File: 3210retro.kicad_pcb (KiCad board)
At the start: 2 copper layers, 44 x 115 mm, 24 parts, among them P109 Rumble_Pads, Q201 BC817-40, Q801 BSS138, SW701 SW_PUSH, SW702 C, SW703 1, SW704 4ghi, SW705 7pqrs, SW706 -, SW707 2abc, SW708 5jkl, SW709 8tuv, SW710 UP, SW711 3def, SW712 6mno, SW713 9wxyz, SW714 *+, SW715 DOWN, SW716 0space, SW717 #up

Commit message: aktuelle Version
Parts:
- added C201: 22p, Capacitors_SMD:C_0603, F.Cu at (225.9, 61.8)
- added C202: 22p, Capacitors_SMD:C_0603, F.Cu at (230.3, 55.9)
- added C203: 22p, Capacitors_SMD:C_0603, F.Cu at (218.9, 67.7)
- added C204: 22p, Capacitors_SMD:C_0603, F.Cu at (192.3, 95.8)
- added C205: C, Capacitors_SMD:C_0603, F.Cu at (196.7, 95.8)
- added C206: C, Capacitors_SMD:C_0603, F.Cu at (210.1, 83.0)
- added C207: 100n, Capacitors_SMD:C_0603, F.Cu at (269.6, 84.1)
- added C208: 100n, Capacitors_SMD:C_0603, F.Cu at (291.1, 67.7)
- added C209: 100n, Capacitors_SMD:C_0603, F.Cu at (274.0, 84.1)
- added C210: 100n, Capacitors_SMD:C_0603, F.Cu at (280.6, 73.6)
- added C211: 100n, Capacitors_SMD:C_0603, F.Cu at (300.3, 55.9)
- added C212: 100n, Capacitors_SMD:C_0603, F.Cu at (282.3, 67.7)
- added C213: 100n, Capacitors_SMD:C_0603, F.Cu at (295.5, 61.8)
- added C214: 100n, Capacitors_SMD:C_0603, F.Cu at (300.4, 85.4)
- added C215: 100n, Capacitors_SMD:C_0603, F.Cu at (307.0, 79.5)
- added C216: 100n, Capacitors_SMD:C_0603, F.Cu at (304.8, 85.4)
- added C217: 100n, Capacitors_SMD:C_0603, F.Cu at (287.2, 85.4)
- added C218: 100n, Capacitors_SMD:C_0603, F.Cu at (247.3, 84.0)
- added C219: 100n, Capacitors_SMD:C_0603, F.Cu at (282.3, 61.8)
- added C220: 100n, Capacitors_SMD:C_0603, F.Cu at (265.2, 80.5)
- added C221: 100n, Capacitors_SMD:C_0603, F.Cu at (256.1, 89.5)
- added C222: 100n, Capacitors_SMD:C_0603, F.Cu at (275.0, 72.3)
- added C223: 100n, Capacitors_SMD:C_0603, F.Cu at (251.7, 89.5)
- added C224: 100n, Capacitors_SMD:C_0603, F.Cu at (307.0, 73.6)
- added C225: 100n, Capacitors_SMD:C_0603, F.Cu at (287.1, 55.9)
- added C226: 10u, Capacitors_SMD:C_0603, F.Cu at (267.4, 74.6)
- added C227: 100n, Capacitors_SMD:C_0603, F.Cu at (291.5, 55.9)
- added C228: 1n, Capacitors_SMD:C_0603, F.Cu at (286.7, 61.8)
- added C229: 1u, Capacitors_SMD:C_0603, F.Cu at (271.8, 78.2)
- added C230: 1u, Capacitors_SMD:C_0603, F.Cu at (291.1, 61.8)
- added C231: 1u, Capacitors_SMD:C_0603, F.Cu at (295.9, 55.9)
- added C301: 100n, Capacitors_SMD:C_0603, F.Cu at (263.4, 126.8)
- added C302: 100n, Capacitors_SMD:C_0603, F.Cu at (258.7, 132.7)
- added C303: 100n, Capacitors_SMD:C_0603, F.Cu at (252.3, 134.9)
- added C304: 100n, Capacitors_SMD:C_0603, F.Cu at (264.4, 115.0)
- added C305: 100n, Capacitors_SMD:C_0603, F.Cu at (247.6, 138.3)
- added C306: 100n, Capacitors_SMD:C_0603, F.Cu at (243.2, 138.3)
- added C307: 100n, Capacitors_SMD:C_0603, F.Cu at (254.6, 123.1)
- added C308: 100n, Capacitors_SMD:C_0603, F.Cu at (254.6, 155.3)
- added C309: 100n, Capacitors_SMD:C_0603, F.Cu at (247.7, 168.1)
- added C310: 100n, Capacitors_SMD:C_0603, F.Cu at (259.0, 155.3)
- added C311: 100n, Capacitors_SMD:C_0603, F.Cu at (243.3, 168.1)
- added C402: 10u, Capacitors_SMD:C_0603, F.Cu at (276.2, 78.2)
- added C403: C, Capacitors_SMD:C_0603, F.Cu at (286.7, 67.7)
- added C405: 100n, Capacitors_SMD:C_0603, F.Cu at (260.8, 80.5)
- added C406: 1n, Capacitors_SMD:C_0603, F.Cu at (265.2, 86.4)
- added C408: 100n, Capacitors_SMD:C_0603, F.Cu at (293.8, 79.5)
- added C409: 100n, Capacitors_SMD:C_0603, F.Cu at (298.2, 73.6)
- added C411: C_Small, Capacitors_SMD:C_0603, F.Cu at (261.9, 74.6)
- added C412: C_Small, Capacitors_SMD:C_0603, F.Cu at (281.6, 55.9)
- added C413: 22p, Capacitors_SMD:C_0603, F.Cu at (285.0, 73.6)
- added C415: 100n, Capacitors_SMD:C_0603, F.Cu at (293.8, 73.6)
- added C701: 1p, Capacitors_SMD:C_0603, F.Cu at (182.2, 143.0)
- added C702: 2p4, Capacitors_SMD:C_0603, F.Cu at (191.6, 133.6)
- added C703: 1u, Capacitors_SMD:C_0603, F.Cu at (208.9, 115.0)
- added C704: 10u, Capacitors_SMD:C_0603, F.Cu at (213.3, 115.0)
- added C705: 100n, Capacitors_SMD:C_0603, F.Cu at (201.5, 130.2)
- added C801: 100n, Capacitors_SMD:C_0603, F.Cu at (348.1, 67.7)
- added C802: 470u, Capacitors_SMD:C_0603, F.Cu at (356.9, 55.9)
- added C803: 100n, Capacitors_SMD:C_0603, F.Cu at (352.5, 67.7)
- added C804: C, Capacitors_SMD:C_0603, F.Cu at (352.5, 61.8)
- added C805: C, Capacitors_SMD:C_0603, F.Cu at (361.3, 55.9)
- added C806: C, Capacitors_SMD:C_0603, F.Cu at (337.8, 74.6)
- added C807: C, Capacitors_SMD:C_0603, F.Cu at (348.1, 61.8)
- added C901: 10n, Capacitors_SMD:C_0603, F.Cu at (165.6, 152.3)
- added C902: 10n, Capacitors_SMD:C_0603, F.Cu at (174.2, 152.3)
- added C903: 10u, Capacitors_SMD:C_0603, F.Cu at (264.4, 120.9)
- added C904: 100n, Capacitors_SMD:C_0603, F.Cu at (268.8, 115.0)
- added D701: LED, LEDs:LED_0603, F.Cu at (313.4, 109.8)
- added D702: LED, LEDs:LED_0603, F.Cu at (317.8, 109.8)
- added D703: LED, LEDs:LED_0603, F.Cu at (322.2, 98.0)
- added D704: LED, LEDs:LED_0603, F.Cu at (322.2, 108.2)
- added D705: LED, LEDs:LED_0603, F.Cu at (322.2, 103.1)
- added D706: LED, LEDs:LED_0603, F.Cu at (310.0, 116.7)
- added L301: 100R, Resistors_SMD:R_0603, F.Cu at (259.0, 149.4)
- added L302: 100R, Resistors_SMD:R_0603, F.Cu at (254.6, 149.4)
- added L401: 4u7, Resistors_SMD:R_0603, F.Cu at (299.8, 67.7)
- added L402: 4u7, Resistors_SMD:R_0603, F.Cu at (304.2, 61.8)
- added L701: 1n3, Resistors_SMD:R_0603, F.Cu at (169.9, 152.3)
- added L702: 2n2, Resistors_SMD:R_0603, F.Cu at (177.9, 143.0)
- added L703: 0, Resistors_SMD:R_0603, F.Cu at (161.3, 152.3)
- added L704: 1n8, Resistors_SMD:R_0603, F.Cu at (208.8, 120.9)
- added P102: BAT, Pin_Headers:Pin_Header_Straight_2x01, F.Cu at (153.0, 165.7)
- added P103: DC, Pin_Headers:Pin_Header_Straight_2x01, F.Cu at (153.0, 173.9)
- added P105: EAR, Pin_Headers:Pin_Header_Straight_2x01, F.Cu at (159.7, 165.7)
- added P106: MIC, Pin_Headers:Pin_Header_Straight_2x01, F.Cu at (159.7, 173.9)
- added P107: HEADPHONE, Pin_Headers:Pin_Header_Straight_1x04, F.Cu at (141.7, 165.7)
- added P108: LSPK, Pin_Headers:Pin_Header_Straight_1x02, F.Cu at (148.6, 165.7)
- added P701: WL_DBG, Pin_Headers:Pin_Header_Straight_1x02, F.Cu at (148.2, 118.2)
- added P702: WL_RS232, Pin_Headers:Pin_Header_Straight_1x03, F.Cu at (141.0, 118.2)
- added P703: BT_DBG, Pin_Headers:Pin_Header_Straight_1x02, F.Cu at (140.0, 131.5)
- added P801: JTAG, Pin_Headers:Pin_Header_Straight_2x05_Pitch1.27mm, F.Cu at (139.0, 55.7)
- added Q301: BC849, TO_SOT_Packages_SMD:SOT-23, F.Cu at (238.4, 168.4)
- added R201: 10, Resistors_SMD:R_0603, F.Cu at (187.9, 93.3)
- added R202: 10, Resistors_SMD:R_0603, F.Cu at (183.5, 99.2)
- added R203: 10, Resistors_SMD:R_0603, F.Cu at (225.9, 55.9)
- added R204: 10, Resistors_SMD:R_0603, F.Cu at (214.5, 65.3)
- added R205: 10, Resistors_SMD:R_0603, F.Cu at (194.6, 89.9)
- added R206: 10, Resistors_SMD:R_0603, F.Cu at (199.0, 89.9)
- added R207: 100, Resistors_SMD:R_0603, F.Cu at (214.5, 71.2)
- added R208: 100, Resistors_SMD:R_0603, F.Cu at (187.9, 99.2)
- added R209: 10k, Resistors_SMD:R_0603, F.Cu at (152.1, 102.6)
- added R210: 10k, Resistors_SMD:R_0603, F.Cu at (210.1, 65.3)
- added R211: 100, Resistors_SMD:R_0603, F.Cu at (194.6, 84.0)
- added R212: 100, Resistors_SMD:R_0603, F.Cu at (205.7, 71.2)
- added R213: 100, Resistors_SMD:R_0603, F.Cu at (221.5, 55.9)
- added R214: 100, Resistors_SMD:R_0603, F.Cu at (199.0, 84.0)
- added R215: 100, Resistors_SMD:R_0603, F.Cu at (156.5, 102.6)
- added R216: 100, Resistors_SMD:R_0603, F.Cu at (160.9, 102.6)
- added R217: 100, Resistors_SMD:R_0603, F.Cu at (212.2, 88.9)
- added R218: 100, Resistors_SMD:R_0603, F.Cu at (169.7, 102.6)
- added R219: 100, Resistors_SMD:R_0603, F.Cu at (205.7, 65.3)
- added R220: 100, Resistors_SMD:R_0603, F.Cu at (183.5, 93.3)
- added R221: 100, Resistors_SMD:R_0603, F.Cu at (147.7, 102.6)
- added R222: 100, Resistors_SMD:R_0603, F.Cu at (214.5, 83.0)
- added R223: R, Resistors_SMD:R_0603, F.Cu at (221.0, 85.4)
- added R224: R, Resistors_SMD:R_0603, F.Cu at (216.6, 88.9)
- added R225: 100, Resistors_SMD:R_0603, F.Cu at (232.1, 73.6)
- added R226: 100, Resistors_SMD:R_0603, F.Cu at (165.3, 102.6)
- added R227: 10k, Resistors_SMD:R_0603, F.Cu at (174.1, 102.6)
- added R228: 100, Resistors_SMD:R_0603, F.Cu at (203.4, 94.8)
- added R229: 100, Resistors_SMD:R_0603, F.Cu at (210.1, 77.1)
- added R230: 100, Resistors_SMD:R_0603, F.Cu at (178.5, 102.6)
- added R231: 100, Resistors_SMD:R_0603, F.Cu at (232.1, 67.7)
- added R232: 100, Resistors_SMD:R_0603, F.Cu at (223.3, 73.6)
- added R233: 100, Resistors_SMD:R_0603, F.Cu at (227.7, 67.7)
- added R234: 100, Resistors_SMD:R_0603, F.Cu at (214.5, 77.1)
- added R235: 100, Resistors_SMD:R_0603, F.Cu at (223.3, 79.5)
- added R236: 100, Resistors_SMD:R_0603, F.Cu at (203.4, 88.9)
- added R237: 100, Resistors_SMD:R_0603, F.Cu at (187.3, 105.1)
- added R238: 100, Resistors_SMD:R_0603, F.Cu at (196.7, 101.7)
- added R239: 100, Resistors_SMD:R_0603, F.Cu at (205.7, 83.0)
- added R240: 100, Resistors_SMD:R_0603, F.Cu at (207.8, 88.9)
- added R241: 100, Resistors_SMD:R_0603, F.Cu at (218.9, 79.5)
- added R242: 100, Resistors_SMD:R_0603, F.Cu at (182.9, 105.1)
- added R243: 100, Resistors_SMD:R_0603, F.Cu at (227.7, 73.6)
- added R244: 100, Resistors_SMD:R_0603, F.Cu at (207.8, 94.8)
- added R245: 100, Resistors_SMD:R_0603, F.Cu at (201.1, 100.7)
- added R246: 100, Resistors_SMD:R_0603, F.Cu at (221.5, 61.8)
- added R247: 100, Resistors_SMD:R_0603, F.Cu at (210.1, 71.2)
- added R248: 100, Resistors_SMD:R_0603, F.Cu at (205.7, 77.1)
- added R249: 0, Resistors_SMD:R_0603, F.Cu at (282.8, 85.4)
- added R301: 4k7, Resistors_SMD:R_0603, F.Cu at (259.0, 167.1)
- added R302: 0, Resistors_SMD:R_0603, F.Cu at (263.4, 161.2)
- added R303: 0, Resistors_SMD:R_0603, F.Cu at (267.8, 155.3)
- added R304: 22, Resistors_SMD:R_0603, F.Cu at (254.6, 167.1)
- added R305: 100, Resistors_SMD:R_0603, F.Cu at (259.0, 161.2)
- added R306: 100, Resistors_SMD:R_0603, F.Cu at (263.4, 155.3)
- added R307: 100, Resistors_SMD:R_0603, F.Cu at (267.8, 149.4)
- added R308: 100, Resistors_SMD:R_0603, F.Cu at (263.4, 149.4)
- added R309: 100, Resistors_SMD:R_0603, F.Cu at (254.6, 161.2)
- added R401: R, Resistors_SMD:R_0603, F.Cu at (289.4, 79.5)
- added R402: R, Resistors_SMD:R_0603, F.Cu at (278.4, 85.4)
- added R403: R, Resistors_SMD:R_0603, F.Cu at (304.7, 55.9)
- added R404: R, Resistors_SMD:R_0603, F.Cu at (295.5, 67.7)
- added R405: R, Resistors_SMD:R_0603, F.Cu at (299.9, 61.8)
- added R406: R, Resistors_SMD:R_0603, F.Cu at (285.0, 79.5)
- added R407: R, Resistors_SMD:R_0603, F.Cu at (289.4, 73.6)
- added R408: R, Resistors_SMD:R_0603, F.Cu at (302.6, 73.6)
- added R409: R, Resistors_SMD:R_0603, F.Cu at (280.6, 79.5)
- added R410: R, Resistors_SMD:R_0603, F.Cu at (296.0, 85.4)
- added R412: R, Resistors_SMD:R_0603, F.Cu at (302.6, 79.5)
- added R413: R, Resistors_SMD:R_0603, F.Cu at (291.6, 85.4)
- added R414: R, Resistors_SMD:R_0603, F.Cu at (298.2, 79.5)
- added R415: R, Resistors_SMD:R_0603, F.Cu at (260.8, 86.4)
- added R416: 0, Resistors_SMD:R_0603, F.Cu at (304.1, 67.7)
- added R601: 100, Resistors_SMD:R_0603, F.Cu at (197.1, 124.3)
- added R602: 100, Resistors_SMD:R_0603, F.Cu at (201.5, 124.3)
- added R701: 10k, Resistors_SMD:R_0603, F.Cu at (301.2, 117.1)
- added R702: 280, Resistors_SMD:R_0603, F.Cu at (313.4, 104.3)
- added R703: 0, Resistors_SMD:R_0603, F.Cu at (197.1, 130.2)
- added R704: 280, Resistors_SMD:R_0603, F.Cu at (305.6, 117.1)
- added R705: 0, Resistors_SMD:R_0603, F.Cu at (200.4, 142.0)
- added R706: 280, Resistors_SMD:R_0603, F.Cu at (313.4, 98.4)
- added R707: 0, Resistors_SMD:R_0603, F.Cu at (191.6, 139.5)
- added R708: 280, Resistors_SMD:R_0603, F.Cu at (296.8, 117.1)
- added R709: 0, Resistors_SMD:R_0603, F.Cu at (205.9, 132.7)
- added R710: 280, Resistors_SMD:R_0603, F.Cu at (317.8, 98.4)
- added R711: 100k, Resistors_SMD:R_0603, F.Cu at (210.3, 126.8)
- added R712: 280, Resistors_SMD:R_0603, F.Cu at (317.8, 104.3)
- added R801: 22, Resistors_SMD:R_0603, F.Cu at (352.5, 73.6)
- added R802: 100, Resistors_SMD:R_0603, F.Cu at (361.3, 73.6)
- added R803: 100, Resistors_SMD:R_0603, F.Cu at (356.9, 73.6)
- added R804: 100, Resistors_SMD:R_0603, F.Cu at (351.0, 79.5)
- added R805: 100, Resistors_SMD:R_0603, F.Cu at (361.3, 67.7)
- added R806: 100, Resistors_SMD:R_0603, F.Cu at (346.6, 79.5)
- added R807: 100, Resistors_SMD:R_0603, F.Cu at (356.9, 67.7)
- added R808: 100, Resistors_SMD:R_0603, F.Cu at (361.3, 61.8)
- added R809: 100, Resistors_SMD:R_0603, F.Cu at (348.1, 73.6)
- added R810: 100, Resistors_SMD:R_0603, F.Cu at (355.4, 79.5)
- added R811: 1M, Resistors_SMD:R_0603, F.Cu at (356.9, 61.8)
- added R812: 0, Resistors_SMD:R_0603, F.Cu at (348.1, 55.9)
- added R813: 100, Resistors_SMD:R_0603, F.Cu at (342.2, 74.6)
- added R814: 0, Resistors_SMD:R_0603, F.Cu at (352.5, 55.9)
- added R815: 0, Resistors_SMD:R_0603, F.Cu at (230.3, 61.8)
- added R816: 100, Resistors_SMD:R_0603, F.Cu at (218.9, 73.6)
- added R817: 100, Resistors_SMD:R_0603, F.Cu at (223.3, 67.7)
- added R818: 100, Resistors_SMD:R_0603, F.Cu at (192.3, 101.7)
- added R901: 100, Resistors_SMD:R_0603, F.Cu at (196.0, 142.0)
- added R902: 100, Resistors_SMD:R_0603, F.Cu at (205.9, 126.8)
- added R903: 100, Resistors_SMD:R_0603, F.Cu at (187.4, 148.9)
- added R904: R, Resistors_SMD:R_0603, F.Cu at (200.4, 136.1)
- added R905: 100, Resistors_SMD:R_0603, F.Cu at (213.1, 120.9)
- added R906: 100, Resistors_SMD:R_0603, F.Cu at (183.0, 148.9)
- added R907: 100, Resistors_SMD:R_0603, F.Cu at (196.0, 136.1)
- added R908: 100, Resistors_SMD:R_0603, F.Cu at (178.6, 148.9)
- added R909: 100, Resistors_SMD:R_0603, F.Cu at (186.6, 143.0)
- added R910: 10k, Resistors_SMD:R_0603, F.Cu at (254.3, 129.0)
- added R911: 10, Resistors_SMD:R_0603, F.Cu at (259.0, 126.8)
- added R912: 10, Resistors_SMD:R_0603, F.Cu at (268.8, 120.9)
- added R913: 10, Resistors_SMD:R_0603, F.Cu at (260.0, 120.9)
- added R914: 22, Resistors_SMD:R_0603, F.Cu at (243.5, 132.4)
- added R915: 10, Resistors_SMD:R_0603, F.Cu at (260.0, 115.0)
- added R916: 10, Resistors_SMD:R_0603, F.Cu at (247.9, 132.4)
- added RP901: 100, Resistors_SMD:R_Array_Convex_8x0602, F.Cu at (255.1, 116.1)
- added RP902: 100, Resistors_SMD:R_Array_Convex_8x0602, F.Cu at (232.9, 134.7)
- added RP903: 100, Resistors_SMD:R_Array_Convex_8x0602, F.Cu at (244.0, 125.4)
- added RP904: 100, Resistors_SMD:R_Array_Convex_8x0602, F.Cu at (249.4, 125.4)
- added RP905: 100, Resistors_SMD:R_Array_Convex_8x0602, F.Cu at (238.3, 134.7)
- added TP201: TP, buttons:TP, F.Cu at (270.0, 66.9)
- added TP202: TP, buttons:TP, F.Cu at (247.9, 57.5)
- added TP203: TP, buttons:TP, F.Cu at (242.3, 76.2)
- added TP204: TP, buttons:TP, F.Cu at (247.9, 76.2)
- added TP205: TP, buttons:TP, F.Cu at (242.3, 57.5)
- added TP206: TP, buttons:TP, F.Cu at (258.9, 57.5)
- added TP207: TP, buttons:TP, F.Cu at (264.5, 57.5)
- added TP208: TP, buttons:TP, F.Cu at (270.0, 57.5)
- added TP209: TP, buttons:TP, F.Cu at (275.6, 57.5)
- added TP210: TP, buttons:TP, F.Cu at (258.9, 66.9)
- added TP211: TP, buttons:TP, F.Cu at (264.5, 66.9)
- added TP212: TP, buttons:TP, F.Cu at (253.4, 66.9)
- added TP213: TP, buttons:TP, F.Cu at (242.3, 85.6)
- added TP214: TP, buttons:TP, F.Cu at (242.3, 66.9)
- added TP215: TP, buttons:TP, F.Cu at (253.4, 57.5)
- added TP216: TP, buttons:TP, F.Cu at (247.9, 66.9)
- added TP301: TP, buttons:TP, F.Cu at (233.0, 151.0)
- added TP302: TP, buttons:TP, F.Cu at (227.4, 160.4)
- added TP303: TP, buttons:TP, F.Cu at (233.0, 160.4)
- added TP304: TP, buttons:TP, F.Cu at (238.5, 151.0)
- added TP305: TP, buttons:TP, F.Cu at (221.9, 169.7)
- added TP306: TP, buttons:TP, F.Cu at (249.6, 160.4)
- added TP307: TP, buttons:TP, F.Cu at (221.9, 151.0)
- added TP308: TP, buttons:TP, F.Cu at (244.1, 160.4)
- added TP309: TP, buttons:TP, F.Cu at (233.0, 169.7)
- added TP310: TP, buttons:TP, F.Cu at (227.4, 169.7)
- added TP311: TP, buttons:TP, F.Cu at (238.5, 160.4)
- added TP312: TP, buttons:TP, F.Cu at (249.6, 151.0)
- added TP313: TP, buttons:TP, F.Cu at (227.4, 151.0)
- added TP314: TP, buttons:TP, F.Cu at (244.1, 151.0)
- added TP315: TP, buttons:TP, F.Cu at (221.9, 160.4)
- added TP501: TP, buttons:TP, F.Cu at (315.4, 57.5)
- added TP502: TP, buttons:TP, F.Cu at (337.6, 66.9)
- added TP503: TP, buttons:TP, F.Cu at (326.5, 76.2)
- added TP504: TP, buttons:TP, F.Cu at (321.0, 76.2)
- added TP505: TP, buttons:TP, F.Cu at (332.1, 66.9)
- added TP506: TP, buttons:TP, F.Cu at (343.1, 57.5)
- added TP507: TP, buttons:TP, F.Cu at (337.6, 57.5)
- added TP508: TP, buttons:TP, F.Cu at (343.1, 66.9)
- added TP509: TP, buttons:TP, F.Cu at (332.1, 57.5)
- added TP510: TP, buttons:TP, F.Cu at (326.5, 66.9)
- added TP511: TP, buttons:TP, F.Cu at (321.0, 66.9)
- added TP512: TP, buttons:TP, F.Cu at (326.5, 57.5)
- added TP513: TP, buttons:TP, F.Cu at (315.4, 76.2)
- added TP514: TP, buttons:TP, F.Cu at (321.0, 57.5)
- added TP515: TP, buttons:TP, F.Cu at (315.4, 66.9)
- added TP601: TP, buttons:TP, F.Cu at (167.5, 144.6)
- added TP602: TP, buttons:TP, F.Cu at (186.6, 125.9)
- added TP701: TP, buttons:TP, F.Cu at (186.6, 135.2)
- added TP702: TP, buttons:TP, F.Cu at (173.0, 144.6)
- added TP703: TP, buttons:TP, F.Cu at (192.2, 125.9)
- added TP704: TP, buttons:TP, F.Cu at (204.0, 116.6)
- added TP705: TP, buttons:TP, F.Cu at (198.4, 116.6)
- added TP706: TP, buttons:TP, F.Cu at (181.1, 135.2)
- added TP707: TP, buttons:TP, F.Cu at (192.9, 116.6)
- added TP708: TP, buttons:TP, F.Cu at (175.5, 135.2)
- added TP709: TP, buttons:TP, F.Cu at (151.4, 136.7)
- added TP710: TP, buttons:TP, F.Cu at (147.8, 127.3)
- added TP711: TP, buttons:TP, F.Cu at (145.3, 146.0)
- added TP712: TP, buttons:TP, F.Cu at (150.8, 146.0)
- added TP713: TP, buttons:TP, F.Cu at (164.5, 135.2)
- added TP714: TP, buttons:TP, F.Cu at (170.0, 135.2)
- added TP715: TP, buttons:TP, F.Cu at (156.4, 146.0)
- added TP716: TP, buttons:TP, F.Cu at (187.3, 116.6)
- added TP717: TP, buttons:TP, F.Cu at (181.1, 125.9)
- added TP718: TP, buttons:TP, F.Cu at (161.9, 144.6)
- added TP719: TP, buttons:TP, F.Cu at (181.8, 116.6)
- added TP720: TP, buttons:TP, F.Cu at (175.5, 125.9)
- added TP721: TP, buttons:TP, F.Cu at (176.3, 116.6)
- added TP722: TP, buttons:TP, F.Cu at (170.7, 116.6)
- added TP723: TP, buttons:TP, F.Cu at (139.8, 140.6)
- added TP724: TP, buttons:TP, F.Cu at (170.0, 125.9)
- added TP725: TP, buttons:TP, F.Cu at (164.5, 125.9)
- added TP726: TP, buttons:TP, F.Cu at (158.9, 125.9)
- added TP727: TP, buttons:TP, F.Cu at (165.2, 116.6)
- added TP728: TP, buttons:TP, F.Cu at (159.6, 116.6)
- added TP729: TP, buttons:TP, F.Cu at (145.8, 136.7)
- added TP730: TP, buttons:TP, F.Cu at (153.4, 127.3)
- added TP731: TP, buttons:TP, F.Cu at (158.9, 135.2)
- added TP732: TP, buttons:TP, F.Cu at (154.1, 116.6)
- added TP733: TP, buttons:TP, F.Cu at (139.8, 150.0)
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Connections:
- net /Buttons and LEDs/COL_1 renamed /Buttons and LEDs/KEY0
- net /Buttons and LEDs/COL_2 renamed /Buttons and LEDs/KEY1
- net /Buttons and LEDs/COL_3 renamed /Buttons and LEDs/KEY2
- net /Buttons and LEDs/COL_4 renamed /Buttons and LEDs/KEY3
- net /Buttons and LEDs/ROW_1 renamed /Buttons and LEDs/KEY4
- net /Buttons and LEDs/ROW_2 renamed /Buttons and LEDs/KEY5
- net /Buttons and LEDs/ROW_3 renamed /Buttons and LEDs/KEY6
- net /Buttons and LEDs/ROW_4 renamed /Buttons and LEDs/KEY7
- P109 pad 1: (no net) -> /Audio Amplifier/RMBL+
- P109 pad 2: (no net) -> +3V3

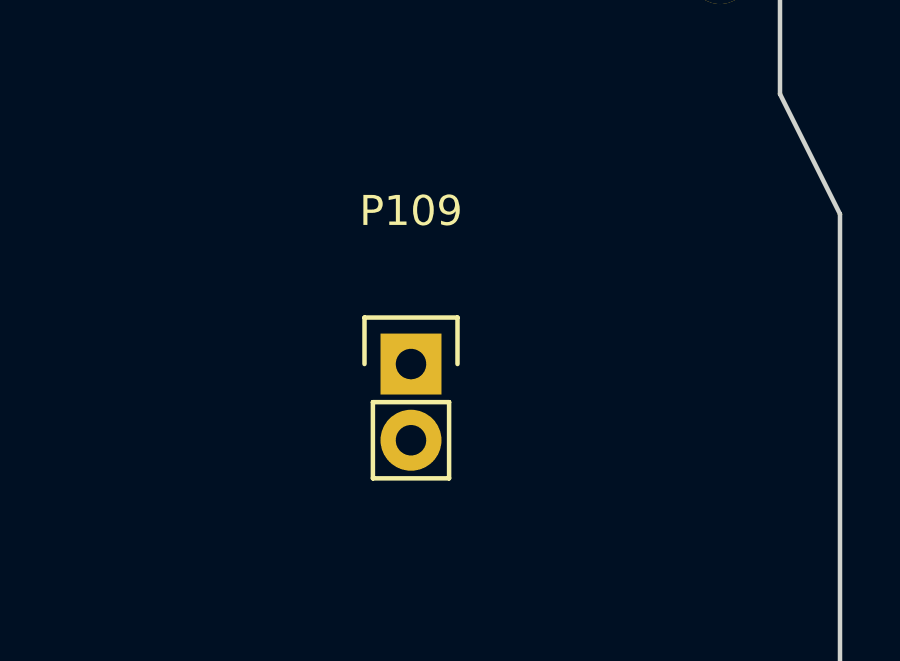
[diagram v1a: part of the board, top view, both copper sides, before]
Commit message: display placement
The placement of the display connector is set.
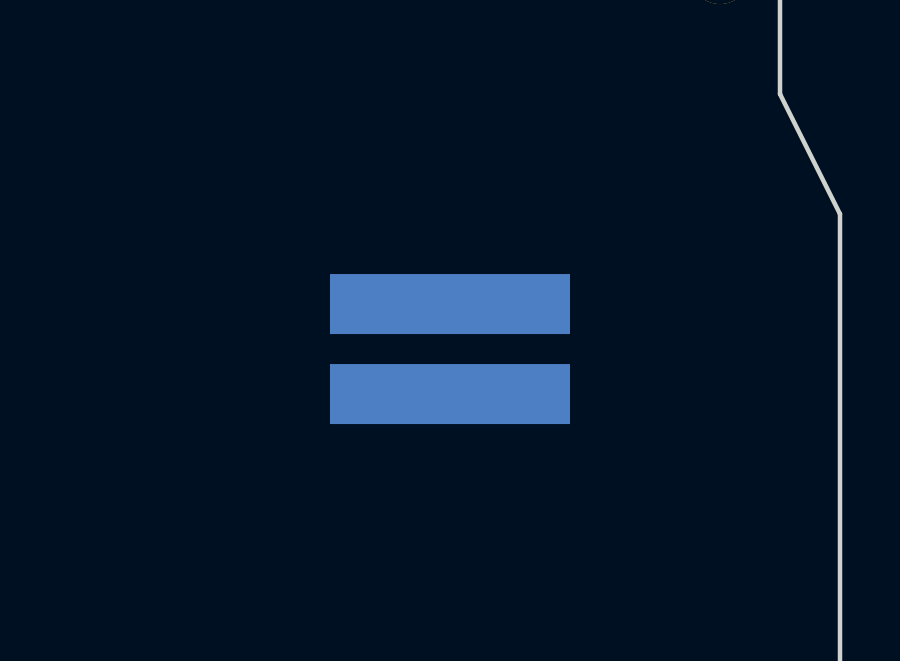
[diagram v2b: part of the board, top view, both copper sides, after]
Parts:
- P109: footprint Pin_Headers:Pin_Header_Straight_1x02 -> buttons:Rumble_Pads; moved to B.Cu
- moved P109 1.64 mm to (108.4, 72.1)
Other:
- board text added: "display ffc connector"
- board text added: "keepout with components"
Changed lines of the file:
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@@
-(kicad_pcb (version 4) (host pcbnew 4.0.2+dfsg1-stable)
+(kicad_pcb (version 4) (host pcbnew 4.0.5)
   (general
     (links 384)
     (no_connects 384)
-    (area 77.314756 44.02184 121.464758 159.171842)
+    (area 57.563473 22.546841 363.4359 175.884842)
     (thickness 1.6)
-    (drawings 26)
+    (drawings 42)
     (tracks 0)
     (zones 0)
@@
     (aux_axis_origin 0 0)
     (grid_origin 79.589757 159.096841)
-    (visible_elements FFFFF77F)
+    (visible_elements 7FFFFFFF)
     (pcbplotparams
       (layerselection 0x00030_80000001)
@@
       (net 413 "Net-(U702-Pad2)") (solder_mask_margin 0.01) (clearance 0.01))
   )
-  (module Pin_Headers:Pin_Header_Straight_1x02 locked (layer F.Cu)
-    (at 107.089757 71.096841)
-    (descr "Through hole pin header")
-    (tags "pin header")
-    (fp_text reference P109 (at 0 -5.1) (layer F.SilkS)
-      (effects (font (size 1 1) (thickness 0.15)))
-    )
-    (fp_text value RUMBLE (at 0 -3.1) (layer F.Fab)
-      (effects (font (size 1 1) (thickness 0.15)))
-    )
-    (fp_line (start 1.27 1.27) (end 1.27 3.81) (layer F.SilkS) (width 0.15))
-    (fp_line (start 1.55 -1.55) (end 1.55 0) (layer F.SilkS) (width 0.15))
-    (fp_line (start -1.75 -1.75) (end -1.75 4.3) (layer F.CrtYd) (width 0.05))
-    (fp_line (start 1.75 -1.75) (end 1.75 4.3) (layer F.CrtYd) (width 0.05))
-    (fp_line (start -1.75 -1.75) (end 1.75 -1.75) (layer F.CrtYd) (width 0.05))
-    (fp_line (start -1.75 4.3) (end 1.75 4.3) (layer F.CrtYd) (width 0.05))
-    (fp_line (start 1.27 1.27) (end -1.27 1.27) (layer F.SilkS) (width 0.15))
-    (fp_line (start -1.55 0) (end -1.55 -1.55) (layer F.SilkS) (width 0.15))
-    (fp_line (start -1.55 -1.55) (end 1.55 -1.55) (layer F.SilkS) (width 0.15))
-    (fp_line (start -1.27 1.27) (end -1.27 3.81) (layer F.SilkS) (width 0.15))
-    (fp_line (start -1.27 3.81) (end 1.27 3.81) (layer F.SilkS) (width 0.15))
-    (pad 1 thru_hole rect (at 0 0) (size 2.032 2.032) (drill 1.016) (layers *.Cu *.Mask F.SilkS)
-      (net 49 "/Audio Amplifier/RMBL+"))
-    (pad 2 thru_hole oval (at 0 2.54) (size 2.032 2.032) (drill 1.016) (layers *.Cu *.Mask F.SilkS)
-      (net 17 +3V3))
-    (model Pin_Headers.3dshapes/Pin_Header_Straight_1x02.wrl
-      (at (xyz 0 -0.05 0))
-      (scale (xyz 1 1 1))
-      (rotate (xyz 0 0 90))
-    )
-  )
   (module buttons:TP (layer F.Cu)
     (at 270.018118 66.889961)
@@
       (net 411 "Net-(TP912-Pad1)"))
   )
+  (module buttons:Rumble_Pads locked (layer B.Cu)
+    (at 108.389757 72.096841)
+    (fp_text reference P109 (at 2.9 -2.5) (layer Dwgs.User)
+      (effects (font (size 0.5 0.5) (thickness 0.125)))
+    )
+    (fp_text value RUMBLE (at 0 0.5) (layer B.Fab)
+      (effects (font (size 0.5 0.5) (thickness 0.125)) (justify mirror))
+    )
+    (pad 1 connect rect (at 0 0) (size 8 2) (layers B.Cu B.Mask)
+      (net 49 "/Audio Amplifier/RMBL+"))
+    (pad 2 connect rect (at 0 -3) (size 8 2) (layers B.Cu B.Mask)
+      (net 17 +3V3))
+  )
+  (gr_text "display ffc connector" (at 96.489757 67.696841) (layer F.CrtYd)
+    (effects (font (size 0.5 0.5) (thickness 0.125)))
+  )
+  (gr_text "keepout with components" (at 94.889757 62.096841) (layer F.CrtYd)
+    (effects (font (size 0.5 0.5) (thickness 0.125)))
+  )
+  (gr_line (start 81.389757 65.696841) (end 81.389757 60.696841) (angle 90) (layer F.CrtYd) (width 0.2))
+  (gr_line (start 117.389757 65.696841) (end 81.389757 65.696841) (angle 90) (layer F.CrtYd) (width 0.2))
+  (gr_line (start 117.389757 60.696841) (end 117.389757 65.696841) (angle 90) (layer F.CrtYd) (width 0.2))
+  (gr_line (start 81.389757 60.696841) (end 117.389757 60.696841) (angle 90) (layer F.CrtYd) (width 0.2))
+  (gr_line (start 110.889757 63.096841) (end 109.389757 63.096841) (angle 90) (layer F.CrtYd) (width 0.2))
+  (gr_line (start 110.889757 73.096841) (end 110.889757 63.096841) (angle 90) (layer F.CrtYd) (width 0.2))
+  (gr_line (start 109.389757 73.096841) (end 110.889757 73.096841) (angle 90) (layer F.CrtYd) (width 0.2))
+  (gr_line (start 87.889757 73.096841) (end 89.389757 73.096841) (angle 90) (layer F.CrtYd) (width 0.2))
+  (gr_line (start 87.889757 63.096841) (end 87.889757 73.096841) (angle 90) (layer F.CrtYd) (width 0.2))
+  (gr_line (start 89.389757 63.096841) (end 87.889757 63.096841) (angle 90) (layer F.CrtYd) (width 0.2))
+  (gr_line (start 109.389757 63.096841) (end 89.389757 63.096841) (angle 90) (layer F.CrtYd) (width 0.2))
+  (gr_line (start 109.389757 73.096841) (end 109.389757 63.096841) (angle 90) (layer F.CrtYd) (width 0.2))
+  (gr_line (start 89.389757 73.096841) (end 109.389757 73.096841) (angle 90) (layer F.CrtYd) (width 0.2))
+  (gr_line (start 89.389757 63.096841) (end 89.389757 73.096841) (angle 90) (layer F.CrtYd) (width 0.2))
   (dimension 115.062 (width 0.3) (layer Dwgs.User)
     (gr_text "115,062 mm" (at 64.777757 101.565841 270) (layer Dwgs.User)

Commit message: Removed WiFi Module added Footprints
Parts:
- removed C701: 1p, Capacitors_SMD:C_0603
- removed C702: 2p4, Capacitors_SMD:C_0603
- removed C703: 1u, Capacitors_SMD:C_0603
- removed C704: 10u, Capacitors_SMD:C_0603
- removed C705: 100n, Capacitors_SMD:C_0603
- removed L701: 1n3, Resistors_SMD:R_0603
- removed L702: 2n2, Resistors_SMD:R_0603
- removed L703, R703, R705, R707, R709: 0, Resistors_SMD:R_0603
- removed L704: 1n8, Resistors_SMD:R_0603
- removed P106: MIC, Pin_Headers:Pin_Header_Straight_2x01
- removed P108: LSPK, Pin_Headers:Pin_Header_Straight_1x02
- removed P701: WL_DBG, Pin_Headers:Pin_Header_Straight_1x02
- removed P702: WL_RS232, Pin_Headers:Pin_Header_Straight_1x03
- removed P703: BT_DBG, Pin_Headers:Pin_Header_Straight_1x02
- removed Q301: BC849, TO_SOT_Packages_SMD:SOT-23
- removed R230, R231, R232, R233: 100, Resistors_SMD:R_0603
- removed R711: 100k, Resistors_SMD:R_0603
- removed REF** (x2): MountingHole_2mm, Mounting_Holes:MountingHole_2-5mm
- removed REF** (x2): MountingHole_4mm, Mounting_Holes:MountingHole_4mm
- removed TP303, TP304, TP305, TP306, TP307, TP308, TP309, TP310, TP311, TP312, TP313, TP314, TP315, TP710, TP711, TP712, TP713, TP714, TP715, TP716, TP717, TP718, TP719, TP720, TP721, TP722, TP723, TP724, TP725, TP726, TP727, TP728, TP729, TP730, TP731, TP732, TP733: TP, buttons:TP
- removed U701, U702: U.FL, buttons:Foil_Button
- added C312: 1u, Capacitors_SMD:C_0603, F.Cu at (284.7, 308.2)
- added C401: 10n, Capacitors_SMD:C_0603, F.Cu at (296.7, 246.6)
- added C404: 1u, Capacitors_SMD:C_0603, F.Cu at (303.3, 241.5)
- added C407: 1u, Capacitors_SMD:C_0603, F.Cu at (289.2, 253.7)
- added C410: 10n, Capacitors_SMD:C_0603, F.Cu at (305.0, 236.5)
- added C414: 22p, Capacitors_SMD:C_0603, F.Cu at (299.1, 241.5)
- added C416: 22p, Capacitors_SMD:C_0603, F.Cu at (292.4, 248.7)
- added C417: 1u, Capacitors_SMD:C_0603, F.Cu at (288.2, 248.7)
- added C418: 1u, Capacitors_SMD:C_0603, F.Cu at (292.3, 236.5)
- added C419: 220u, Capacitors_SMD:C_0603, F.Cu at (294.8, 241.5)
- added C420: 1u, Capacitors_SMD:C_0603, F.Cu at (300.9, 246.6)
- added C421: 1u, Capacitors_SMD:C_0603, F.Cu at (300.8, 236.5)
- added C422: 220u, Capacitors_SMD:C_0603, F.Cu at (284.9, 253.7)
- added C423: 100n, Capacitors_SMD:C_0603, F.Cu at (296.5, 236.5)
- added C424: 100n, Capacitors_SMD:C_0603, F.Cu at (283.9, 248.7)
- added C425: 100n, Capacitors_SMD:C_0603, F.Cu at (290.6, 243.6)
- added C426: 100n, Capacitors_SMD:C_0603, F.Cu at (286.3, 243.6)
- added D301: D_Schottky, Diodes_SMD:D_0603, F.Cu at (282.6, 302.4)
- added FB401: FILTER, Choke_SMD:Choke_SMD_1206_Standard, F.Cu at (287.4, 237.5)
- added FB402: FILTER, Choke_SMD:Choke_SMD_1206_Standard, F.Cu at (279.0, 248.0)
- added FI401: EMI_FILTER2, Choke_SMD:Choke_SMD_1206_Standard, F.Cu at (142.6, 255.5)
- added J901: MICRO_SD, Connectors_Hirose:microSD_Card_Receptacle_Hirose_DM3AT-SF-PEJM5, B.Cu at (93.8, 148.8)
- added L303: 18u, Resistors_SMD:R_0603, F.Cu at (282.5, 313.2)
- added P101: USB_OTG, Connectors_Molex:USB_Micro-B_Molex_47346-0001, B.Cu at (106.6, 156.3)
- added P301: SEPS525, buttons:FFC-05-35, F.Cu at (90.8, 71.1)
- added R310: 100, Resistors_SMD:R_0603, F.Cu at (288.9, 308.2)
- added R311: 100, Resistors_SMD:R_0603, F.Cu at (282.6, 318.2)
- added R312: 100, Resistors_SMD:R_0603, F.Cu at (297.4, 302.3)
- added R313: 100, Resistors_SMD:R_0603, F.Cu at (286.7, 313.2)
- added R314: 100, Resistors_SMD:R_0603, F.Cu at (276.1, 324.1)
- added R315: 100, Resistors_SMD:R_0603, F.Cu at (293.2, 307.3)
- added R316: 100, Resistors_SMD:R_0603, F.Cu at (282.6, 323.2)
- added R317: 100, Resistors_SMD:R_0603, F.Cu at (297.4, 307.3)
- added R318: 100, Resistors_SMD:R_0603, F.Cu at (293.2, 312.3)
- added R319: 100, Resistors_SMD:R_0603, F.Cu at (286.9, 318.2)
- added R320: 100, Resistors_SMD:R_0603, F.Cu at (293.2, 302.3)
- added R321: 100, Resistors_SMD:R_0603, F.Cu at (271.9, 321.9)
- added R322: 100, Resistors_SMD:R_0603, F.Cu at (278.4, 319.1)
- added R323: 10k, Resistors_SMD:R_0603, F.Cu at (291.1, 317.3)
- added R411: 50k, Resistors_SMD:R_0603, F.Cu at (297.7, 251.6)
- added R417: 50k, Resistors_SMD:R_0603, F.Cu at (305.2, 246.5)
- added R418: 100k, Resistors_SMD:R_0603, F.Cu at (306.2, 251.5)
- added R419: 1k, Resistors_SMD:R_0603, F.Cu at (293.4, 253.7)
- added R420: 1k, Resistors_SMD:R_0603, F.Cu at (301.9, 251.6)
- added U201: STM32F439NIH6, buttons:STM32F439NI, F.Cu at (99.3, 83.6)
- added U302: TPS61041DBV, TO_SOT_Packages_SMD:SOT-23, F.Cu at (258.1, 311.2)
- added U403: DRV8601, buttons:DRV8601, F.Cu at (279.3, 254.1)
- added U404: LM4930, buttons:QFN-44-1EP_7x7mm_Pitch0.5mm, F.Cu at (270.1, 239.7)
- added U405: TS5A22366, buttons:TS5A22366, F.Cu at (271.0, 248.9)
- added U406: MP34DT01TR, buttons:MP34DT01, F.Cu at (270.8, 254.6)
- added U407: MP34DT01TR, buttons:MP34DT01, F.Cu at (279.3, 242.2)
- added U801: A7, buttons:A7, B.Cu at (99.0, 98.3)
- added U802: SIM_SLOT, buttons:SIM, B.Cu at (99.5, 79.4)
- added U901: ESP-12E, buttons:ESP-12E, B.Cu at (98.1, 57.8)
- added X101: ANT_GPS, SMD_Packages:1Pin, F.Cu at (219.7, 308.9)
- added X102: ANT_GSM, SMD_Packages:1Pin, F.Cu at (219.7, 318.2)
- added Y201: 32kHz, Crystals:Crystal_SMD_SeikoEpson_MC146-4pin_6.7x1.5mm_HandSoldering, F.Cu at (143.0, 286.9)
- added Y202: 24MHz, Crystals:Crystal_SMD_SeikoEpson_MC146-4pin_6.7x1.5mm_HandSoldering, F.Cu at (147.6, 276.3)
- added Y401: 1M, Crystals:Crystal_SMD_SeikoEpson_MC146-4pin_6.7x1.5mm_HandSoldering, F.Cu at (279.4, 236.9)
- C310: value 100n -> 4u7C
- C311: value 100n -> 10p
- R301: value 4k7 -> 2M2
- R302: value 0 -> 162k
- R303: value 0 -> 70k
- R304: value 22 -> 5k1
- moved R710 282.7 mm to (140.0, 318.2)
- moved TP745 280.2 mm to (140.9, 324.6)
- moved TP748 276.2 mm to (142.1, 324.6)
- moved R712 273.7 mm to (140.0, 312.3)
- moved R702 272.7 mm to (144.3, 318.2)
- moved TP747 272.1 mm to (139.7, 321.8)
- moved TP739 270.1 mm to (139.7, 323.2)
- moved TP736 269.1 mm to (143.3, 321.8)
- moved TP744 268.8 mm to (138.5, 324.6)
- moved D703 267.7 mm to (161.3, 311.9)
- moved D705 267.7 mm to (161.3, 317.0)
- moved R706 267.5 mm to (152.8, 312.3)
- moved TP735 265.0 mm to (144.5, 321.8)
- moved TP737 264.2 mm to (142.1, 323.2)
- moved TP738 263.5 mm to (138.5, 321.8)
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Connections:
- C310 pad 1: Net-(C310-Pad1) -> +4V
- C311 pad 1: /Display/RST -> +15V
- C311 pad 2: GND -> Net-(C311-Pad2)
- L302 pad 1: /Display/VDDA -> VDD
- P107 pad 4: /Audio Amplifier/HPM -> (no net)
- P109 pad 1: /Audio Amplifier/RMBL+ -> (no net)
- P109 pad 2: +3V3 -> /Audio Amplifier/RMBL+
- P801 pad 7: Net-(P801-Pad7) -> (no net)
- R214 pad 2: /Controller/ESP_UART0 -> (no net)
- R215 pad 2: /Controller/ESP_UART1 -> (no net)
- R216 pad 2: /Controller/ESP_UART2 -> (no net)
- R217 pad 2: /Controller/ESP_UART3 -> (no net)
- R220 pad 2: Net-(R220-Pad2) -> /Controller/CH_PD
- R240 pad 2: /Controller/BL_ON -> (no net)
- R301 pad 1: /Controller/BL_ON -> +15V
- R301 pad 2: Net-(C310-Pad1) -> Net-(C311-Pad2)
- R302 pad 1: +3V3 -> Net-(C311-Pad2)
- R302 pad 2: /Display/LED+ -> GND
- R303 pad 1: +4V -> Net-(P301-Pad5)
- R303 pad 2: /Display/LED+ -> GND
- R304 pad 2: GND -> Net-(P301-Pad6)
- R305 pad 1: /Controller/SCK -> Net-(P301-Pad9)
- R305 pad 2: /Display/SCK -> /Controller/DISPLAY_DATA13
- R306 pad 1: /Controller/SDA -> Net-(P301-Pad10)
- R306 pad 2: /Display/SDA -> /Controller/DISPLAY_DATA14
- R307 pad 1: /Controller/AO -> Net-(P301-Pad11)
- R307 pad 2: /Display/AO -> /Controller/DISPLAY_DATA15
- R308 pad 1: /Controller/CS -> Net-(P301-Pad12)
- R308 pad 2: /Display/CS -> /Controller/DISPLAY_DATA15
- R309 pad 1: /Display/RST_IN -> Net-(P301-Pad13)
- R309 pad 2: /Display/RST -> /Controller/DISPLAY_DATA16
- R601 pad 2: /Controller/GPIO12 -> (no net)
- R602 pad 2: /Controller/GPIO13 -> (no net)
- R801 pad 2: Net-(R801-Pad2) -> /Controller/RADIO_RST
- R803 pad 1: Net-(R803-Pad1) -> (no net)
- R804 pad 1: Net-(R804-Pad1) -> (no net)
- R805 pad 1: Net-(R805-Pad1) -> (no net)
- R806 pad 1: Net-(R806-Pad1) -> (no net)
- R807 pad 1: Net-(R807-Pad1) -> (no net)
- R808 pad 1: Net-(R808-Pad1) -> (no net)
- R809 pad 1: Net-(R809-Pad1) -> (no net)
- R810 pad 1: Net-(R810-Pad1) -> (no net)
- R813 pad 2: Net-(R813-Pad2) -> (no net)
- R905 pad 1: /Controller/ESP_UART2 -> (no net)
- RP901 pad 10: Net-(RP901-Pad10) -> (no net)
- RP901 pad 11: Net-(RP901-Pad11) -> (no net)
- RP901 pad 12: Net-(RP901-Pad12) -> (no net)
- RP901 pad 13: Net-(RP901-Pad13) -> (no net)
- RP901 pad 14: Net-(RP901-Pad14) -> (no net)
- RP901 pad 15: Net-(RP901-Pad15) -> (no net)
- RP901 pad 16: Net-(RP901-Pad16) -> (no net)
- RP901 pad 9: Net-(RP901-Pad9) -> (no net)
- RP902 pad 10: Net-(RP902-Pad10) -> (no net)
- RP902 pad 11: Net-(RP902-Pad11) -> (no net)
- RP902 pad 12: Net-(RP902-Pad12) -> (no net)
- RP902 pad 13: Net-(RP902-Pad13) -> (no net)
- RP902 pad 14: Net-(RP902-Pad14) -> (no net)
- RP902 pad 15: Net-(RP902-Pad15) -> (no net)
- RP902 pad 16: Net-(RP902-Pad16) -> (no net)
- RP902 pad 9: Net-(RP902-Pad9) -> (no net)
- RP903 pad 10: Net-(RP903-Pad10) -> (no net)
- RP903 pad 11: Net-(RP903-Pad11) -> (no net)
- RP903 pad 12: Net-(RP903-Pad12) -> (no net)
- RP903 pad 13: Net-(RP903-Pad13) -> (no net)
- RP903 pad 14: Net-(RP903-Pad14) -> (no net)
- RP903 pad 15: Net-(RP903-Pad15) -> (no net)
- RP903 pad 16: Net-(RP903-Pad16) -> (no net)
- RP903 pad 9: Net-(RP903-Pad9) -> (no net)
- RP904 pad 10: Net-(RP904-Pad10) -> (no net)
- RP904 pad 11: Net-(RP904-Pad11) -> (no net)
- RP904 pad 12: Net-(RP904-Pad12) -> (no net)
- RP904 pad 13: Net-(RP904-Pad13) -> (no net)
- RP904 pad 14: Net-(RP904-Pad14) -> (no net)
- RP904 pad 15: Net-(RP904-Pad15) -> (no net)
- RP904 pad 16: Net-(RP904-Pad16) -> (no net)
- RP904 pad 7: Net-(RP904-Pad7) -> (no net)
- RP904 pad 8: Net-(RP904-Pad8) -> (no net)
- RP904 pad 9: Net-(RP904-Pad9) -> (no net)
- RP905 pad 10: Net-(RP905-Pad10) -> (no net)
- RP905 pad 11: Net-(RP905-Pad11) -> (no net)
- RP905 pad 12: Net-(RP905-Pad12) -> (no net)
- RP905 pad 13: Net-(RP905-Pad13) -> (no net)
- RP905 pad 14: Net-(RP905-Pad14) -> (no net)
- RP905 pad 15: Net-(RP905-Pad15) -> (no net)
- RP905 pad 16: Net-(RP905-Pad16) -> (no net)
- RP905 pad 9: Net-(RP905-Pad9) -> (no net)
- TP203 pad 1: Net-(TP203-Pad1) -> (no net)
- TP301 pad 1: Net-(TP301-Pad1) -> (no net)
- TP302 pad 1: Net-(TP302-Pad1) -> (no net)
- TP502 pad 1: Net-(TP502-Pad1) -> (no net)
- TP503 pad 1: Net-(TP503-Pad1) -> (no net)
- TP504 pad 1: Net-(TP504-Pad1) -> (no net)
- TP505 pad 1: Net-(TP505-Pad1) -> (no net)
- TP506 pad 1: Net-(TP506-Pad1) -> (no net)
- TP507 pad 1: Net-(TP507-Pad1) -> (no net)
- TP508 pad 1: Net-(TP508-Pad1) -> (no net)
- TP509 pad 1: Net-(TP509-Pad1) -> (no net)
- TP511 pad 1: Net-(TP511-Pad1) -> (no net)
- TP512 pad 1: Net-(TP512-Pad1) -> (no net)
- TP513 pad 1: Net-(TP513-Pad1) -> (no net)
- TP514 pad 1: Net-(TP514-Pad1) -> (no net)
- TP515 pad 1: Net-(TP515-Pad1) -> (no net)
- TP601 pad 1: Net-(TP601-Pad1) -> (no net)
- TP602 pad 1: Net-(TP602-Pad1) -> (no net)
- TP701 pad 1: Net-(TP701-Pad1) -> (no net)
- TP702 pad 1: Net-(TP702-Pad1) -> (no net)
- TP703 pad 1: Net-(TP703-Pad1) -> (no net)
- TP704 pad 1: Net-(TP704-Pad1) -> (no net)
- TP707 pad 1: Net-(TP707-Pad1) -> (no net)
- TP708 pad 1: Net-(TP708-Pad1) -> (no net)
- TP709 pad 1: Net-(TP709-Pad1) -> (no net)
- TP735 pad 1: Net-(TP735-Pad1) -> (no net)
- TP736 pad 1: Net-(TP736-Pad1) -> (no net)
- TP737 pad 1: Net-(TP737-Pad1) -> (no net)
- TP738 pad 1: Net-(TP738-Pad1) -> (no net)
- TP739 pad 1: Net-(TP739-Pad1) -> (no net)
- TP740 pad 1: Net-(TP740-Pad1) -> (no net)
- TP741 pad 1: Net-(TP741-Pad1) -> (no net)
- TP742 pad 1: Net-(TP742-Pad1) -> (no net)
- TP743 pad 1: Net-(TP743-Pad1) -> (no net)
- TP744 pad 1: Net-(TP744-Pad1) -> (no net)
- TP745 pad 1: Net-(TP745-Pad1) -> (no net)
- TP746 pad 1: Net-(TP746-Pad1) -> (no net)
- TP747 pad 1: Net-(TP747-Pad1) -> (no net)
- TP748 pad 1: Net-(TP748-Pad1) -> (no net)
- TP801 pad 1: Net-(TP801-Pad1) -> (no net)
- TP802 pad 1: Net-(TP802-Pad1) -> (no net)
- TP803 pad 1: Net-(TP803-Pad1) -> (no net)
- TP804 pad 1: Net-(TP804-Pad1) -> (no net)
- TP805 pad 1: Net-(TP805-Pad1) -> (no net)
- TP806 pad 1: Net-(TP806-Pad1) -> (no net)
- TP807 pad 1: Net-(TP807-Pad1) -> (no net)
- TP808 pad 1: Net-(TP808-Pad1) -> (no net)
- TP826 pad 1: Net-(TP826-Pad1) -> (no net)
- TP827 pad 1: Net-(TP827-Pad1) -> (no net)
- TP828 pad 1: Net-(TP828-Pad1) -> (no net)
- TP829 pad 1: Net-(TP829-Pad1) -> (no net)
- TP830 pad 1: Net-(TP830-Pad1) -> (no net)
- TP831 pad 1: Net-(TP831-Pad1) -> (no net)
- TP832 pad 1: Net-(TP832-Pad1) -> (no net)
- TP833 pad 1: Net-(TP833-Pad1) -> (no net)
- TP834 pad 1: Net-(TP834-Pad1) -> (no net)
- TP835 pad 1: Net-(TP835-Pad1) -> (no net)
- TP836 pad 1: Net-(TP836-Pad1) -> (no net)
- TP837 pad 1: Net-(TP837-Pad1) -> (no net)
- TP838 pad 1: Net-(TP838-Pad1) -> (no net)
- TP839 pad 1: Net-(TP839-Pad1) -> (no net)
- TP840 pad 1: Net-(TP840-Pad1) -> (no net)
- TP841 pad 1: Net-(TP841-Pad1) -> (no net)
- TP842 pad 1: Net-(TP842-Pad1) -> (no net)
- TP843 pad 1: Net-(TP843-Pad1) -> (no net)
- TP844 pad 1: Net-(TP844-Pad1) -> (no net)
- TP845 pad 1: Net-(TP845-Pad1) -> (no net)
- TP846 pad 1: Net-(TP846-Pad1) -> (no net)
- TP847 pad 1: Net-(TP847-Pad1) -> (no net)
- TP848 pad 1: Net-(TP848-Pad1) -> (no net)
- TP849 pad 1: Net-(TP849-Pad1) -> (no net)
- TP850 pad 1: Net-(TP850-Pad1) -> (no net)
- TP851 pad 1: Net-(TP851-Pad1) -> (no net)
- TP852 pad 1: Net-(TP852-Pad1) -> (no net)
- TP853 pad 1: Net-(TP853-Pad1) -> (no net)
- TP854 pad 1: Net-(TP854-Pad1) -> (no net)
- TP855 pad 1: Net-(TP855-Pad1) -> (no net)
- TP856 pad 1: Net-(TP856-Pad1) -> (no net)
- TP901 pad 1: Net-(TP901-Pad1) -> (no net)
- TP902 pad 1: Net-(TP902-Pad1) -> (no net)
- TP903 pad 1: Net-(TP903-Pad1) -> (no net)
- TP904 pad 1: Net-(TP904-Pad1) -> (no net)
- TP905 pad 1: Net-(TP905-Pad1) -> (no net)
- TP906 pad 1: Net-(TP906-Pad1) -> (no net)
- TP907 pad 1: Net-(TP907-Pad1) -> (no net)
- TP908 pad 1: Net-(TP908-Pad1) -> (no net)
- TP909 pad 1: Net-(TP909-Pad1) -> (no net)
- TP910 pad 1: Net-(TP910-Pad1) -> (no net)
- TP911 pad 1: Net-(TP911-Pad1) -> (no net)
- TP912 pad 1: Net-(TP912-Pad1) -> (no net)
